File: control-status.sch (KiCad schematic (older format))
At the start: 11 parts, among them SW1 SW_PUSH, SW2 SW_PUSH, U10 MAX803

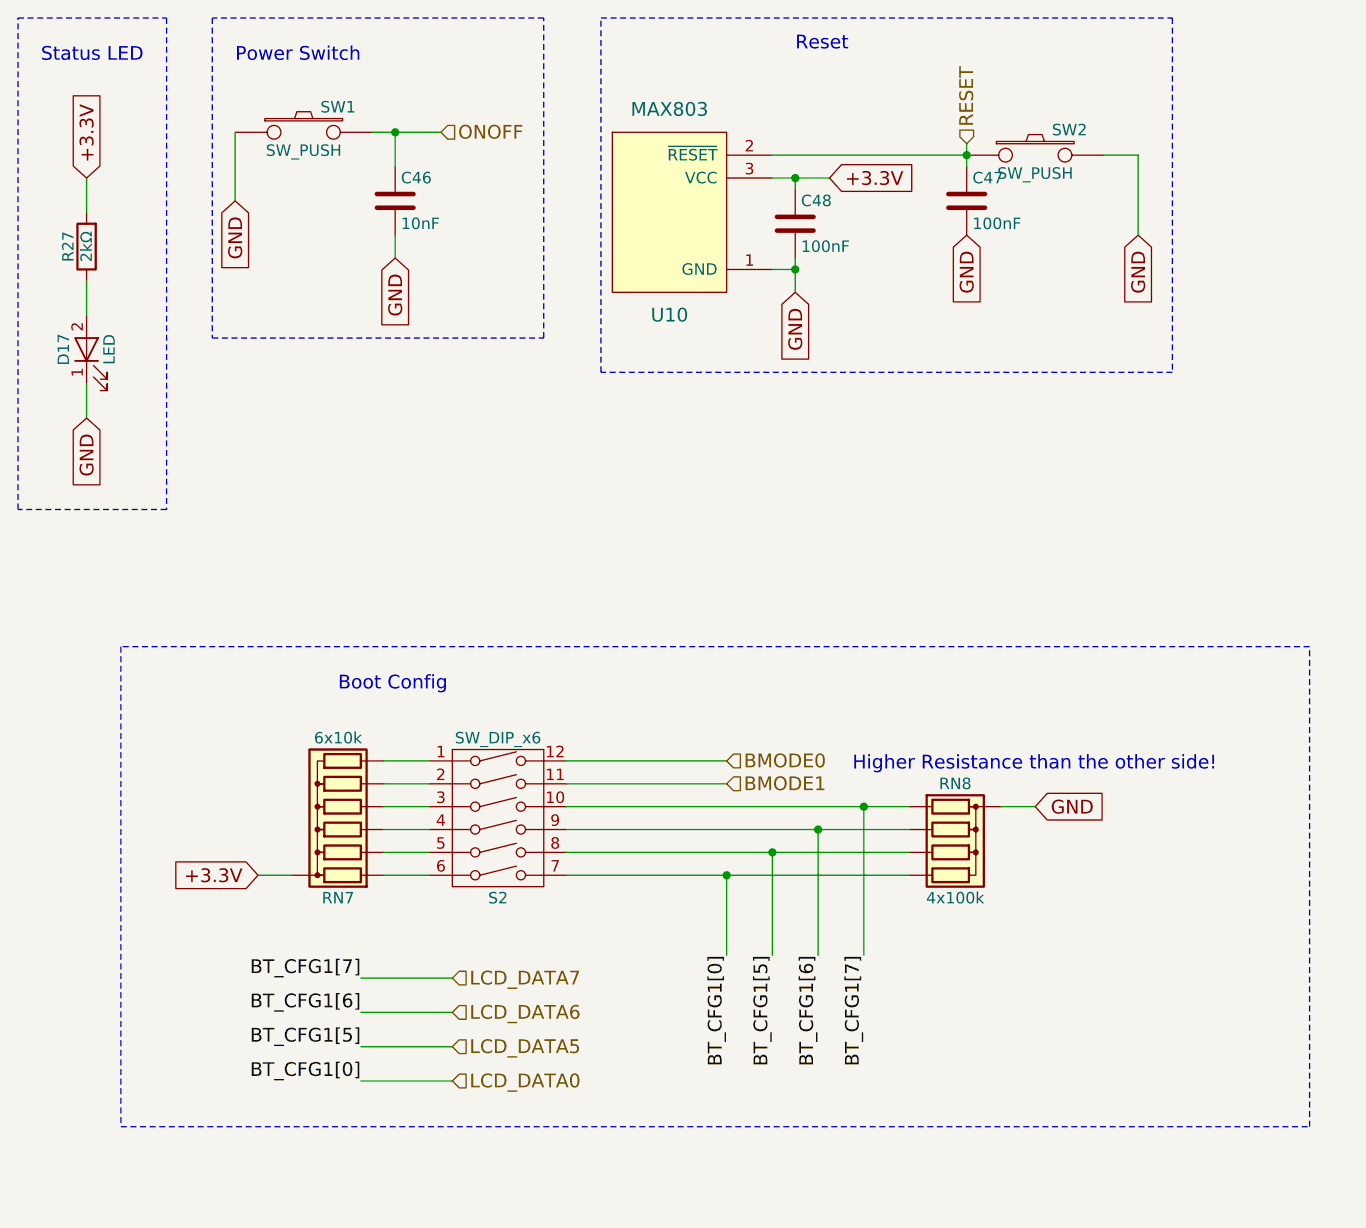
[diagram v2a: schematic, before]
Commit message: I have verified the schematic a second time (except the so-dimm), and I have selected all of the components with links and footprint. I need to verify the schematic a third time and root
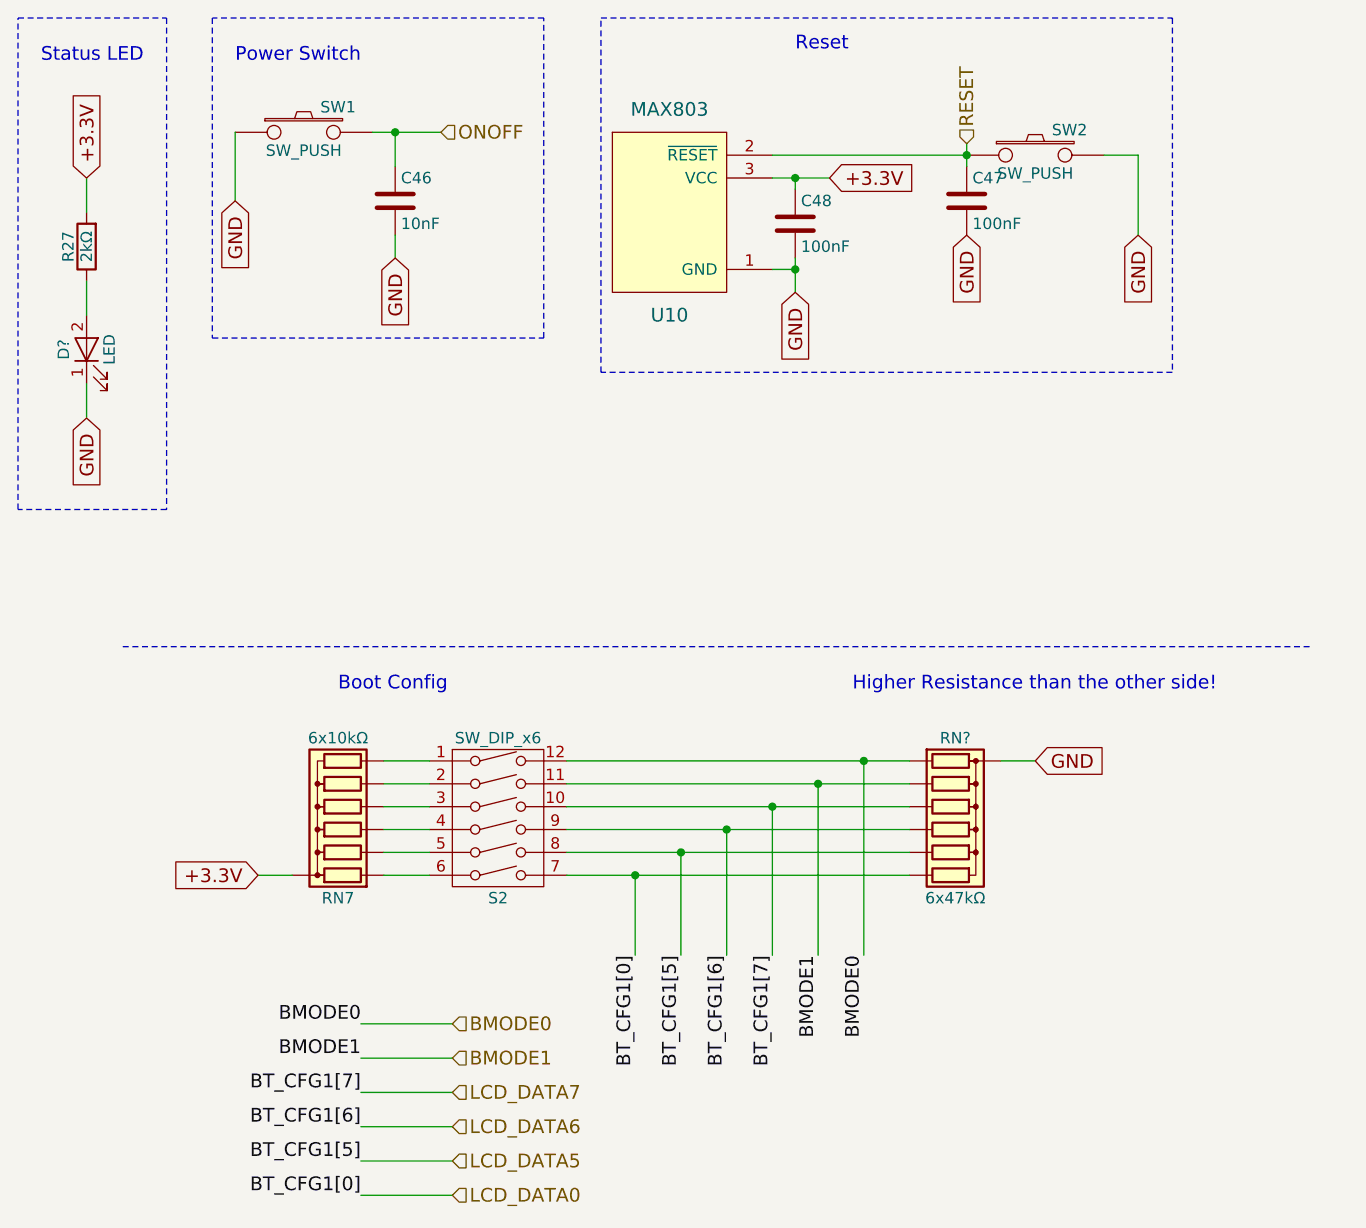
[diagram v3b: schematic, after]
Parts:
- removed D17: LED, symbol LED
- removed RN8: 4x100k, Resistors_THT:R_Array_SIP5, symbol R_Network04
- added D?: LED, LEDs:LED_1206, symbol LED
- added RN?: 6x47kΩ, water:YC158-Yageo-Handsoldering, symbol R_Network06
- RN7: value 6x10k -> 6x10kΩ; footprint Resistors_THT:R_Array_SIP7 -> water:YC158-Yageo-Handsoldering
- S2: footprint (none) -> Housings_DIP:DIP-12_W7.62mm_LongPads
- U10: footprint (none) -> TO_SOT_Packages_SMD:SOT-23
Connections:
- net BMODE0: now also RN?.2 (R1)
- net BMODE1: now also RN?.3 (R2)
- net GND: now also D?.1 (K), RN?.1 (common)
- net LCD_DATA0: now also RN?.7 (R6)
- net LCD_DATA5: now also RN?.6 (R5)
- net LCD_DATA6: now also RN?.5 (R4)
- net LCD_DATA7: now also RN?.4 (R3)
- net at R27.1: now also D?.2 (A)
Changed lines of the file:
@@
 Text Notes 850  950  0    60   ~ 0
 Status LED
-$Comp
-L LED D17
-U 1 1 59A3B634
-P 1050 2200
-F 0 "D17" H 1050 2300 50  0000 C CNN
-F 1 "LED" H 1050 2100 50  0000 C CNN
-F 2 "" H 1050 2200 50  0001 C CNN
-F 3 "" H 1050 2200 50  0001 C CNN
-	1    1050 2200
-	0    -1   -1   0
-$EndComp
 Text Notes 1700 950  0    60   ~ 0
 Power Switch
@@
 F 0 "U10" H 3600 350 60  0000 C CNN
 F 1 "MAX803" H 3600 1250 60  0000 C CNN
-F 2 "" H 3900 1200 60  0001 C CNN
-F 3 "" H 3900 1200 60  0001 C CNN
+F 2 "TO_SOT_Packages_SMD:SOT-23" H 3900 1200 60  0001 C CNN
+F 3 "http://hu.farnell.com/on-semiconductor/max803sq308t1g/reset-3-08vth-0-14-0-46s-act-lw/dp/2318553" H 3900 1200 60  0001 C CNN
 	1    3900 1200
 	1    0    0    -1
@@
 F 0 "S2" H 2850 3900 50  0000 C CNN
 F 1 "SW_DIP_x6" H 2850 4600 50  0000 C CNN
-F 2 "" H 2800 4250 60  0000 C CNN
-F 3 "" H 2800 4250 60  0000 C CNN
+F 2 "Housings_DIP:DIP-12_W7.62mm_LongPads" H 2800 4250 60  0001 C CNN
+F 3 "http://hu.farnell.com/apem/ndir06st/switch-dil-6way/dp/1082468" H 2800 4250 60  0001 C CNN
 	1    2850 4250
 	1    0    0    -1
@@
 P 2150 4200
 F 0 "RN7" V 1750 4200 50  0000 C CNN
-F 1 "6x10k" V 2450 4200 50  0000 C CNN
-F 2 "Resistors_THT:R_Array_SIP7" V 2525 4200 50  0001 C CNN
-F 3 "" H 2150 4200 50  0001 C CNN
+F 1 "6x10kΩ" V 2450 4200 50  0000 C CNN
+F 2 "water:YC158-Yageo-Handsoldering" V 2525 4200 50  0001 C CNN
+F 3 "http://hu.farnell.com/yageo-phycomp/yc158tjr-0710kl/resistor-array-8-10k-0-05-smd/dp/9236236" H 2150 4200 50  0001 C CNN
 	1    2150 4200
 	0    -1   -1   0
@@
 Text GLabel 1800 4500 0    60   Input ~ 0
 +3.3V
-Text HLabel 3850 4000 2    60   Input ~ 0
+Text HLabel 2650 5150 2    60   Input ~ 0
 BMODE0
-Text HLabel 3850 4100 2    60   Input ~ 0
+Text HLabel 2650 5300 2    60   Input ~ 0
 BMODE1
-$Comp
-L R_Network04 RN8
-U 1 1 59A43007
-P 4850 4400
-F 0 "RN8" V 4550 4400 50  0000 C CNN
-F 1 "4x100k" V 5050 4400 50  0000 C CNN
-F 2 "Resistors_THT:R_Array_SIP5" V 5125 4400 50  0001 C CNN
-F 3 "" H 4850 4400 50  0001 C CNN
-	1    4850 4400
-	0    1    1    0
-$EndComp
-Text GLabel 5200 4200 2    60   Input ~ 0
-GND
-Text HLabel 2650 5400 2    60   Input ~ 0
+Text GLabel 5200 4000 2    60   Input ~ 0
+GND
+Text HLabel 2650 5900 2    60   Input ~ 0
 LCD_DATA0
-Text HLabel 2650 5250 2    60   Input ~ 0
+Text HLabel 2650 5750 2    60   Input ~ 0
 LCD_DATA5
-Text HLabel 2650 5100 2    60   Input ~ 0
+Text HLabel 2650 5600 2    60   Input ~ 0
 LCD_DATA6
-Text HLabel 2650 4950 2    60   Input ~ 0
+Text HLabel 2650 5450 2    60   Input ~ 0
 LCD_DATA7
 Wire Wire Line
@@
 	2350 4500 2550 4500
 Wire Wire Line
-	3150 4000 3850 4000
-Wire Wire Line
-	3150 4100 3850 4100
+	3150 4000 4650 4000
+Wire Wire Line
+	3150 4100 4650 4100
 Wire Wire Line
 	3150 4200 4650 4200
@@
 Wire Wire Line
 	3150 4500 4650 4500
-Wire Wire Line
-	5050 4200 5200 4200
-Wire Wire Line
-	3850 4850 3850 4500
-Connection ~ 3850 4500
-Wire Wire Line
-	4050 4850 4050 4400
-Connection ~ 4050 4400
-Wire Wire Line
-	4250 4850 4250 4300
-Connection ~ 4250 4300
-Wire Wire Line
-	4450 4850 4450 4200
-Connection ~ 4450 4200
-Text Notes 4400 4050 0    60   ~ 0
+Text Notes 4400 3700 0    60   ~ 0
 Higher Resistance than the other side!
-Text Label 2250 4950 2    60   ~ 0
+Text Label 2250 5450 2    60   ~ 0
 BT_CFG1[7]
-Text Label 2250 5100 2    60   ~ 0
+Text Label 2250 5600 2    60   ~ 0
 BT_CFG1[6]
-Text Label 2250 5250 2    60   ~ 0
+Text Label 2250 5750 2    60   ~ 0
 BT_CFG1[5]
-Text Label 2250 5400 2    60   ~ 0
+Text Label 2250 5900 2    60   ~ 0
 BT_CFG1[0]
 Wire Wire Line
-	2250 4950 2650 4950
-Wire Wire Line
-	2250 5100 2650 5100
-Wire Wire Line
-	2250 5250 2650 5250
-Wire Wire Line
-	2250 5400 2650 5400
+	2250 5450 2650 5450
+Wire Wire Line
+	2250 5600 2650 5600
+Wire Wire Line
+	2250 5750 2650 5750
+Wire Wire Line
+	2250 5900 2650 5900
+Text Label 3450 4850 3    60   ~ 0
+BT_CFG1[0]
+Text Label 3650 4850 3    60   ~ 0
+BT_CFG1[5]
 Text Label 3850 4850 3    60   ~ 0
-BT_CFG1[0]
+BT_CFG1[6]
 Text Label 4050 4850 3    60   ~ 0
-BT_CFG1[5]
-Text Label 4250 4850 3    60   ~ 0
-BT_CFG1[6]
-Text Label 4450 4850 3    60   ~ 0
 BT_CFG1[7]
 Text Notes 2150 3700 0    60   ~ 0
 Boot Config
-Wire Notes Line
-	1200 3500 1200 5600
-Wire Notes Line
-	1200 5600 6400 5600
-Wire Notes Line
-	6400 5600 6400 3500
 Wire Notes Line
 	6400 3500 1200 3500
@@
 	-1   0    0    1
 $EndComp
+$Comp
+L LED D?
+U 1 1 59AA09A7
+P 1050 2200
+F 0 "D?" H 1050 2300 50  0000 C CNN
+F 1 "LED" H 1050 2100 50  0000 C CNN
+F 2 "LEDs:LED_1206" H 1050 2200 50  0001 C CNN
+F 3 "http://hu.farnell.com/lumex/sml-lx1206gw-tr/led-2mm-x-1-6mm-green-10mcd-565nm/dp/2062262" H 1050 2200 50  0001 C CNN
+	1    1050 2200
+	0    -1   -1   0
+$EndComp
+$Comp
+L R_Network06 RN?
+U 1 1 59AA2AB9
+P 4850 4300
+F 0 "RN?" V 4450 4300 50  0000 C CNN
+F 1 "6x47kΩ" V 5150 4300 50  0000 C CNN
+F 2 "water:YC158-Yageo-Handsoldering" V 5225 4300 50  0001 C CNN
+F 3 "http://hu.farnell.com/yageo-phycomp/yc158tjr-0747kl/resistor-network-rna310-1206-47k/dp/9236279" H 4850 4300 50  0001 C CNN
+	1    4850 4300
+	0    1    1    0
+$EndComp
+Text Label 2250 5150 2    60   ~ 0
+BMODE0
+Text Label 2250 5300 2    60   ~ 0
+BMODE1
+Wire Wire Line
+	2250 5150 2650 5150
+Wire Wire Line
+	2250 5300 2650 5300
+Wire Wire Line
+	5050 4000 5200 4000
+Text Label 4450 4850 3    60   ~ 0
+BMODE0
+Text Label 4250 4850 3    60   ~ 0
+BMODE1
+Wire Wire Line
+	3450 4850 3450 4500
+Connection ~ 3450 4500
+Wire Wire Line
+	3650 4850 3650 4400
+Connection ~ 3650 4400
+Wire Wire Line
+	3850 4850 3850 4300
+Connection ~ 3850 4300
+Wire Wire Line
+	4050 4850 4050 4200
+Connection ~ 4050 4200
+Wire Wire Line
+	4250 4850 4250 4100
+Connection ~ 4250 4100
+Wire Wire Line
+	4450 4850 4450 4000
+Connection ~ 4450 4000
 $EndSCHEMATC

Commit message: part numbers generated;
pcb generation started
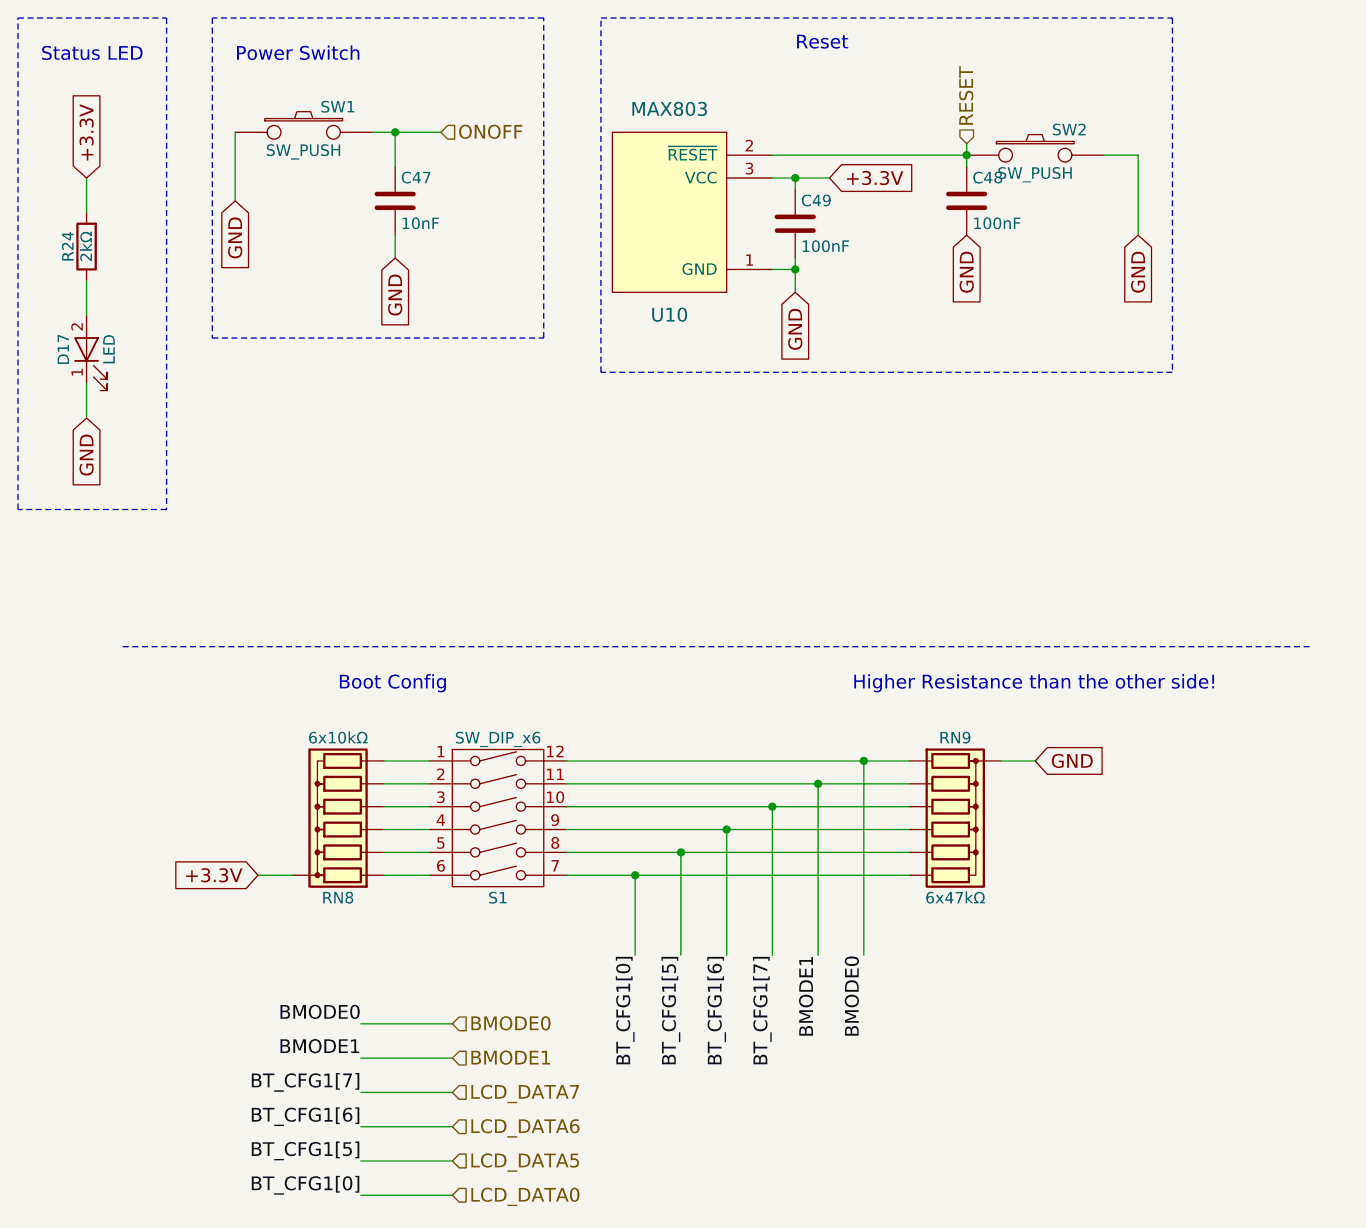
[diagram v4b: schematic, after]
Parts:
- gave numbers to parts that had none: 2
- renumbered C46 to C47, C47 to C48, C48 to C49, R27 to R24, RN7 to RN8, S2 to S1
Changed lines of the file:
@@
 GND
 $Comp
-L C C46
+L C C47
 U 1 1 59A3BB74
 P 2400 1550
-F 0 "C46" H 2425 1650 50  0000 L CNN
+F 0 "C47" H 2425 1650 50  0000 L CNN
 F 1 "10nF" H 2425 1450 50  0000 L CNN
 F 2 "Capacitors_SMD:C_0603_HandSoldering" H 2438 1400 50  0001 C CNN
@@
 +3.3V
 $Comp
-L SW_DIP_x6 S2
+L SW_DIP_x6 S1
 U 1 1 59A40F18
 P 2850 4250
-F 0 "S2" H 2850 3900 50  0000 C CNN
+F 0 "S1" H 2850 3900 50  0000 C CNN
 F 1 "SW_DIP_x6" H 2850 4600 50  0000 C CNN
 F 2 "Housings_DIP:DIP-12_W7.62mm_LongPads" H 2800 4250 60  0001 C CNN
@@
 $EndComp
 $Comp
-L R_Network06 RN7
+L R_Network06 RN8
 U 1 1 59A4135A
 P 2150 4200
-F 0 "RN7" V 1750 4200 50  0000 C CNN
+F 0 "RN8" V 1750 4200 50  0000 C CNN
 F 1 "6x10kΩ" V 2450 4200 50  0000 C CNN
 F 2 "water:YC158-Yageo-Handsoldering" V 2525 4200 50  0001 C CNN
@@
 	6400 3500 1200 3500
 $Comp
-L C C47
+L C C48
 U 1 1 59A6A0B2
 P 4900 1550
-F 0 "C47" H 4925 1650 50  0000 L CNN
+F 0 "C48" H 4925 1650 50  0000 L CNN
 F 1 "100nF" H 4925 1450 50  0000 L CNN
 F 2 "Capacitors_SMD:C_0603_HandSoldering" H 4938 1400 30  0001 C CNN
@@
 $EndComp
 $Comp
-L C C48
+L C C49
 U 1 1 59A6A9F5
 P 4150 1650
-F 0 "C48" H 4175 1750 50  0000 L CNN
+F 0 "C49" H 4175 1750 50  0000 L CNN
 F 1 "100nF" H 4175 1550 50  0000 L CNN
 F 2 "Capacitors_SMD:C_0603_HandSoldering" H 4188 1500 30  0001 C CNN
@@
 $EndComp
 $Comp
-L R R27
+L R R24
 U 1 1 59A95521
 P 1050 1750
-F 0 "R27" V 1130 1750 50  0000 C CNN
+F 0 "R24" V 1130 1750 50  0000 C CNN
 F 1 "2kΩ" V 1050 1750 50  0000 C CNN
 F 2 "Resistors_SMD:R_0603_HandSoldering" V 980 1750 50  0001 C CNN
@@
 $EndComp
 $Comp
-L LED D?
+L LED D17
 U 1 1 59AA09A7
 P 1050 2200
-F 0 "D?" H 1050 2300 50  0000 C CNN
+F 0 "D17" H 1050 2300 50  0000 C CNN
 F 1 "LED" H 1050 2100 50  0000 C CNN
 F 2 "LEDs:LED_1206" H 1050 2200 50  0001 C CNN
@@
 $EndComp
 $Comp
-L R_Network06 RN?
+L R_Network06 RN9
 U 1 1 59AA2AB9
 P 4850 4300
-F 0 "RN?" V 4450 4300 50  0000 C CNN
+F 0 "RN9" V 4450 4300 50  0000 C CNN
 F 1 "6x47kΩ" V 5150 4300 50  0000 C CNN
 F 2 "water:YC158-Yageo-Handsoldering" V 5225 4300 50  0001 C CNN

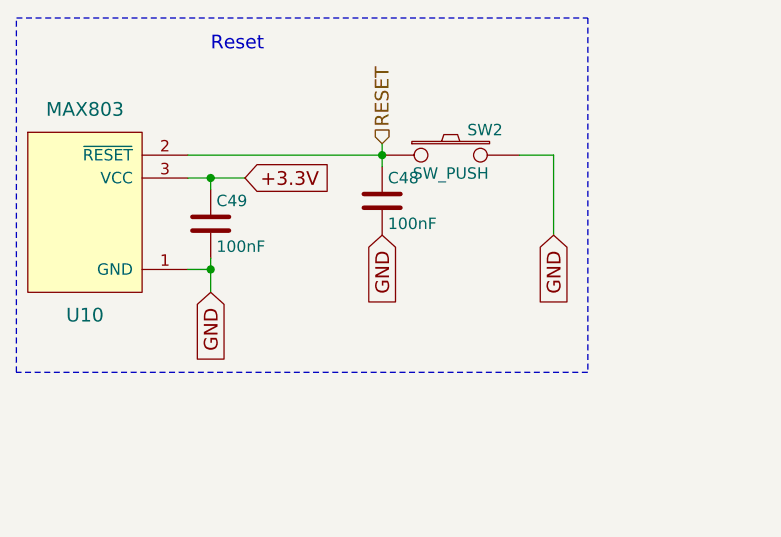
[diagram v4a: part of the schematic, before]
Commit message: I have replaced the normal usb, with a vertical usb.
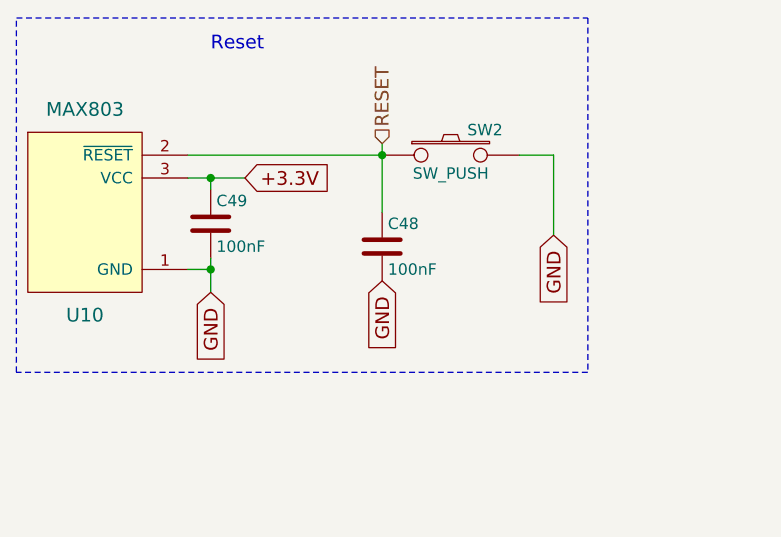
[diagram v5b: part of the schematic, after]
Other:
- moved on the sheet: C48
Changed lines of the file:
@@
 Text GLabel 5650 1700 3    60   Input ~ 0
 GND
-Text GLabel 4900 1700 3    60   Input ~ 0
+Text GLabel 4900 1900 3    60   Input ~ 0
 GND
 Text HLabel 4900 1300 1    60   Input ~ 0
@@
 	4150 1800 4150 1950
 Wire Wire Line
-	4900 1300 4900 1400
+	4900 1300 4900 1600
 Connection ~ 4900 1350
 Wire Wire Line
@@
 L C C48
 U 1 1 59A6A0B2
-P 4900 1550
-F 0 "C48" H 4925 1650 50  0000 L CNN
-F 1 "100nF" H 4925 1450 50  0000 L CNN
-F 2 "Capacitors_SMD:C_0603_HandSoldering" H 4938 1400 30  0001 C CNN
-F 3 "hu.farnell.com/avx/06035c104kat2a/cap-mlcc-x7r-100nf-50v-0603/dp/1301804" H 4900 1550 60  0001 C CNN
-	1    4900 1550
+P 4900 1750
+F 0 "C48" H 4925 1850 50  0000 L CNN
+F 1 "100nF" H 4925 1650 50  0000 L CNN
+F 2 "Capacitors_SMD:C_0603_HandSoldering" H 4938 1600 30  0001 C CNN
+F 3 "hu.farnell.com/avx/06035c104kat2a/cap-mlcc-x7r-100nf-50v-0603/dp/1301804" H 4900 1750 60  0001 C CNN
+	1    4900 1750
 	1    0    0    -1
 $EndComp
